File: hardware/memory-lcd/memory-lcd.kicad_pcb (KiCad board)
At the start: 2 copper layers, 77 x 49 mm, 23 parts, among them J1 NHD-0220FZ, J2 Conn_Mem_Ext, J3 Conn_Power, U1 74HC688, U2 74LVC1G08, U3 MIC5504-3.3YM5, U4 74LVC1G04

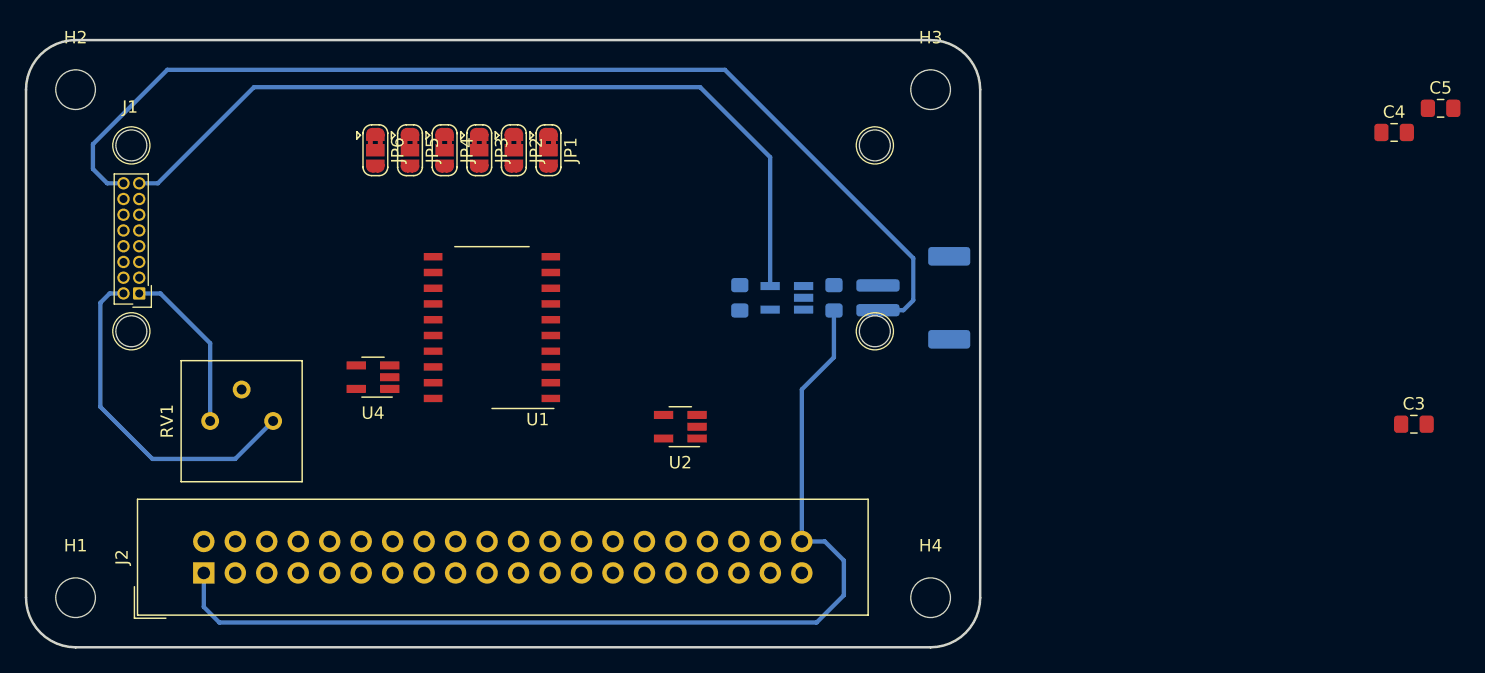
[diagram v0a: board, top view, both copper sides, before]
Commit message: Update all to Kicad 6
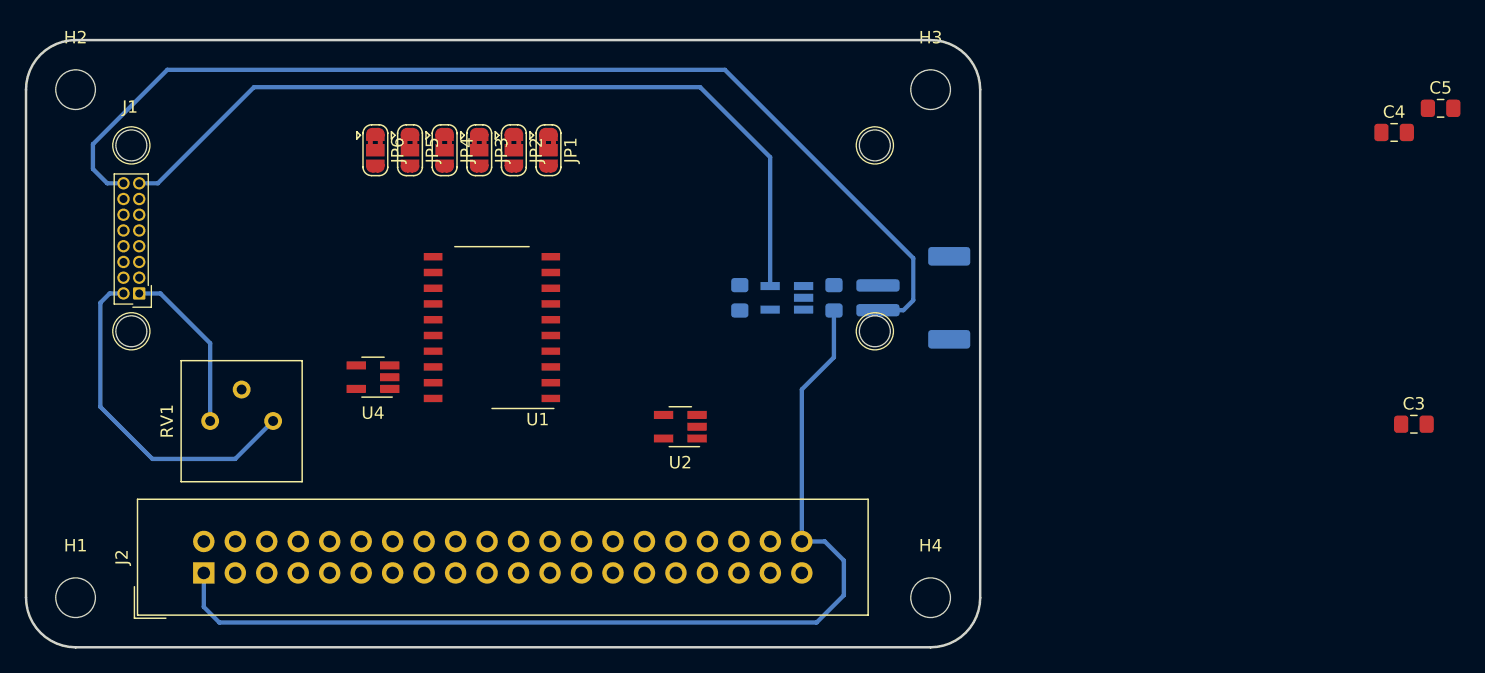
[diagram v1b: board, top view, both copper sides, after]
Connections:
- net /~LCD_E renamed /~{LCD_E}
- net /~MEM_E renamed /~{MEM_E}
- net /~MEM_OE renamed /~{MEM_OE}
- net /~MEM_WE renamed /~{MEM_WE}
- net /~RESET renamed /~{RESET}
- net /~WAIT renamed /~{WAIT}
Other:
- net class Default removed
